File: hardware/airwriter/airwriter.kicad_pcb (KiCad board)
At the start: 2 copper layers, 62 x 104.3 mm, 130 parts, among them J1 USB-C 5V in, J2 Mini-DIN-8 to printer, J4 Mini-DIN-8 LocalTalk, SW1 EVQP44B3M side-press, SW3 TS-1002-BR16026, U1 ESP32-S3-WROOM-1-N8R2, U2 MAX3490ESA+, U3 MAX3232ESE+, U4 AP7361C-33E, U5 USBLC6-2SC6, U6 SP3485EN-L, U7 PIC12F1840-I/P, U8 SP3485EN-L, U9 74AHCT1G125SE-7

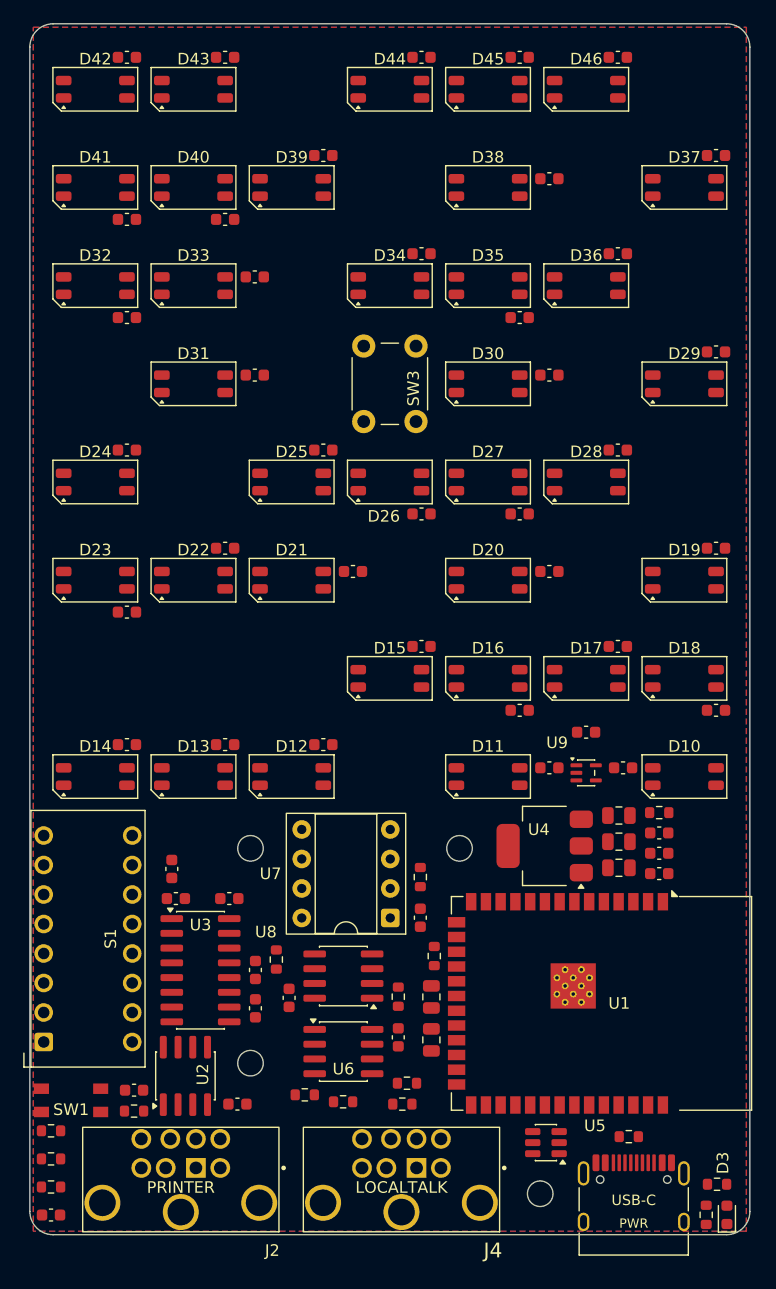
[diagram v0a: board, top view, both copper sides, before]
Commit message: Line the LED caps up for the light grille
All 37 bypass caps sit at one offset, 2.6mm north of their LED, inside
the grille cell and clear of the lattice walls; the LED designators
join the passives on F.Fab, which is what un-crowds the cells.

Refs: W-573
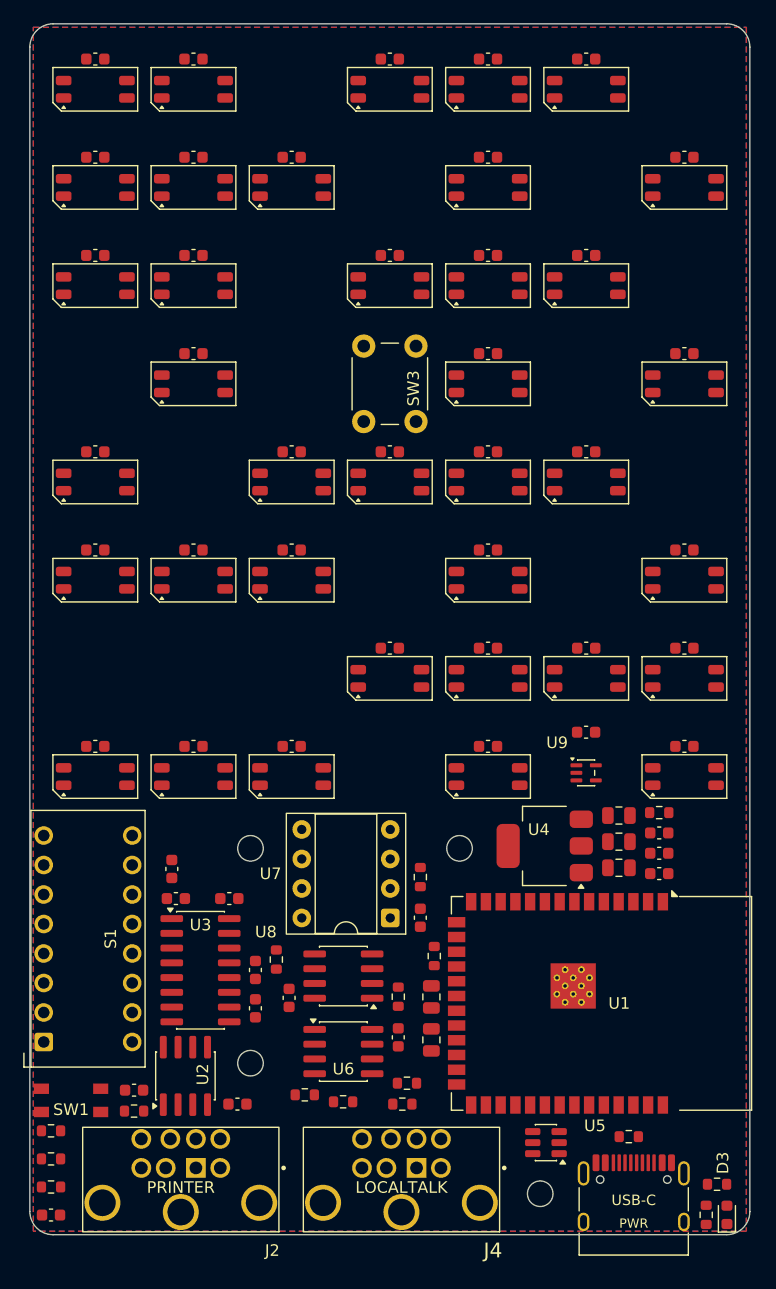
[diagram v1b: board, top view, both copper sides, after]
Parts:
- moved C38 6.00 mm to (156.4, 113.8)
- moved C55 6.00 mm to (139.5, 79.9)
- moved C60 6.00 mm to (114.1, 71.5)
- moved C36 6.00 mm to (139.5, 113.8)
- moved C46 6.00 mm to (131.0, 96.9)
- moved C47 6.00 mm to (139.5, 96.9)
- moved C52 6.00 mm to (105.6, 79.9)
- moved C61 6.00 mm to (105.6, 71.5)
- moved C43 6.00 mm to (105.6, 105.3)
- moved C30 5.59 mm to (156.4, 122.2)
- moved C31 5.59 mm to (139.5, 122.2)
- moved C53 5.59 mm to (114.1, 79.9)
- moved C58 5.59 mm to (139.5, 71.5)
- moved C40 5.59 mm to (139.5, 105.3)
- moved C41 5.59 mm to (122.5, 105.3)
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
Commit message: Route the dot-panel board
Full route at 60 passes, zero real breaks, 909 segments, 28 stitching
vias on the re-centred grid (stitch.py's lattice box now follows the
moved WROOM). Battery: 6 benign violations (5 silk-edge, U1's known
lib mismatch), drills at or above 0.30, /VBUS on the 0.5mm class.

Refs: W-573
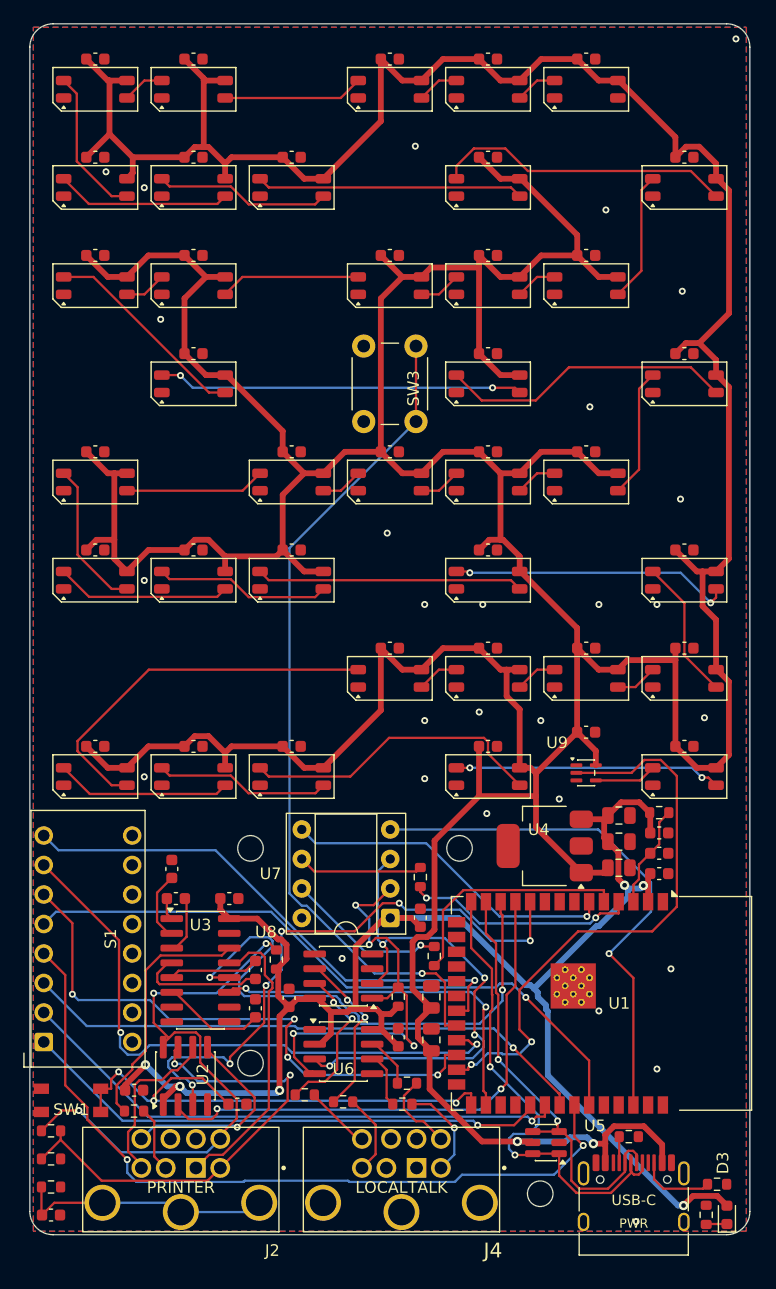
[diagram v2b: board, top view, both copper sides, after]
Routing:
- net /VBUS: track 0.00 -> 539.0 mm, vias 0 -> 2
- net /+3V3: track 0.00 -> 145.9 mm, vias 0 -> 6
- net /BTN_TEST: track 0.00 -> 72.9 mm, vias 0 -> 1
- net /DIP4: track 0.00 -> 66.6 mm, vias 0 -> 2
- net /DIP5: track 0.00 -> 56.8 mm, vias 0 -> 1
- net /DIP7: track 0.00 -> 52.3 mm, vias 0 -> 2
- net /UART_TX: track 0.00 -> 51.0 mm, vias 0 -> 6
- net /LED_DATA: track 0.00 -> 50.0 mm, vias 0 -> 2
- net /PR_TXD_P: track 0.00 -> 49.8 mm, vias 0 -> 3
- net /DIP6: track 0.00 -> 49.8 mm, vias 0 -> 4
- net /DIP3: track 0.00 -> 49.4 mm, vias 0 -> 1
- net /DIP2: track 0.00 -> 48.2 mm, vias 0 -> 1
- net /UART_CTS: track 0.00 -> 47.8 mm, vias 0 -> 2
- net /UART_RX: track 0.00 -> 46.6 mm, vias 0 -> 2
- net /DIP8: track 0.00 -> 46.1 mm, vias 0 -> 1
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
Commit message: Adjust silkscreen labels by hand
Wells repositioned silk labels in KiCad.

Refs: W-573
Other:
- board text added: "APPLETALK"
- board text added: "SERIAL"
- board text added: "TASHTALK"
- board text removed: "LOCALTALK"
- board text removed: "PRINTER"
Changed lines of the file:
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@@
 		(tags "SOIC SO 16-pin-NSOP R-16 R-16-S D0016A M2B SO16 SOT109-1 751B SOIC_N narrow")
 		(property "Reference" "U3"
-			(at 0 -3.9 0)
+			(at 0 0 0)
 			(layer "F.SilkS")
 			(effects
@@
 		(tags "SOIC SO")
 		(property "Reference" "U2"
-			(at 0.130733 1.494292 90)
+			(at 0 0 90)
 			(layer "F.SilkS")
 			(effects
@@
 		(tags "CMS SOT")
 		(property "Reference" "U4"
-			(at 0.51303 1.409538 180)
+			(at 3.135 2.695 180)
 			(layer "F.SilkS")
 			(effects
@@
 		(tags "SOIC SO")
 		(property "Reference" "U6"
-			(at 0 1.5 0)
+			(at 0 0 0)
 			(layer "F.SilkS")
 			(effects
@@
 		(tags "SOIC SO")
 		(property "Reference" "U8"
-			(at 6.678363 3.798133 180)
+			(at 0 0 180)
 			(layer "F.SilkS")
 			(effects
@@
 		(tags "SOT TO_SOT_SMD SC-88A SOT-353 SC-70-5")
 		(property "Reference" "U9"
-			(at -2.5 -2.598077 0)
+			(at -2.5 0 0)
 			(layer "F.SilkS")
 			(effects
@@
 		(tags "DIP switch SPST right angle piano DP-08RP 7.62mm 300mil")
 		(property "Reference" "S1"
-			(at 0 1.955 90)
+			(at 0 0 90)
 			(layer "F.SilkS")
 			(effects
@@
 		(tags "tactile switch side press edge mount EVQP4 C79164")
 		(property "Reference" "SW1"
-			(at 0 -0.8 180)
+			(at 0 0 180)
 			(layer "F.SilkS")
 			(effects
@@
 		(tags "THT DIP DIL PDIP 2.54mm 7.62mm 300mil Socket")
 		(property "Reference" "U7"
-			(at 10.31 3.81 180)
+			(at 3.81 3.81 180)
 			(layer "F.SilkS")
 			(effects
@@
 		(layer "Edge.Cuts")
 	)
-	(gr_text "PWR"
-		(at 152 163.3 0)
+	(gr_text "SERIAL"
+		(at 113 160.2 0)
 		(layer "F.SilkS")
 		(effects
 			(font
-				(size 0.8 0.8)
+				(size 1 1)
 				(thickness 0.15)
 			)
 		)
 	)
-	(gr_text "USB-C"
-		(at 152 161.3 0)
+	(gr_text "TASHTALK"
+		(at 127.2 127.4 0)
 		(layer "F.SilkS")
 		(effects
 			(font
-				(size 0.9 0.9)
+				(size 1 1)
 				(thickness 0.15)
 			)
 		)
 	)
-	(gr_text "PRINTER"
-		(at 113 160.2 0)
+	(gr_text "APPLETALK"
+		(at 132 160.2 0)
 		(layer "F.SilkS")
 		(effects
@@
 		)
 	)
-	(gr_text "LOCALTALK"
-		(at 132 160.2 0)
+	(gr_text "USB-C"
+		(at 152 160.4 0)
+		(layer "F.SilkS")
+		(effects
+			(font
+				(size 1 1)
+				(thickness 0.15)
+			)
+		)
+	)
+	(gr_text "PWR"
+		(at 152 162.12 0)
 		(layer "F.SilkS")
 		(effects

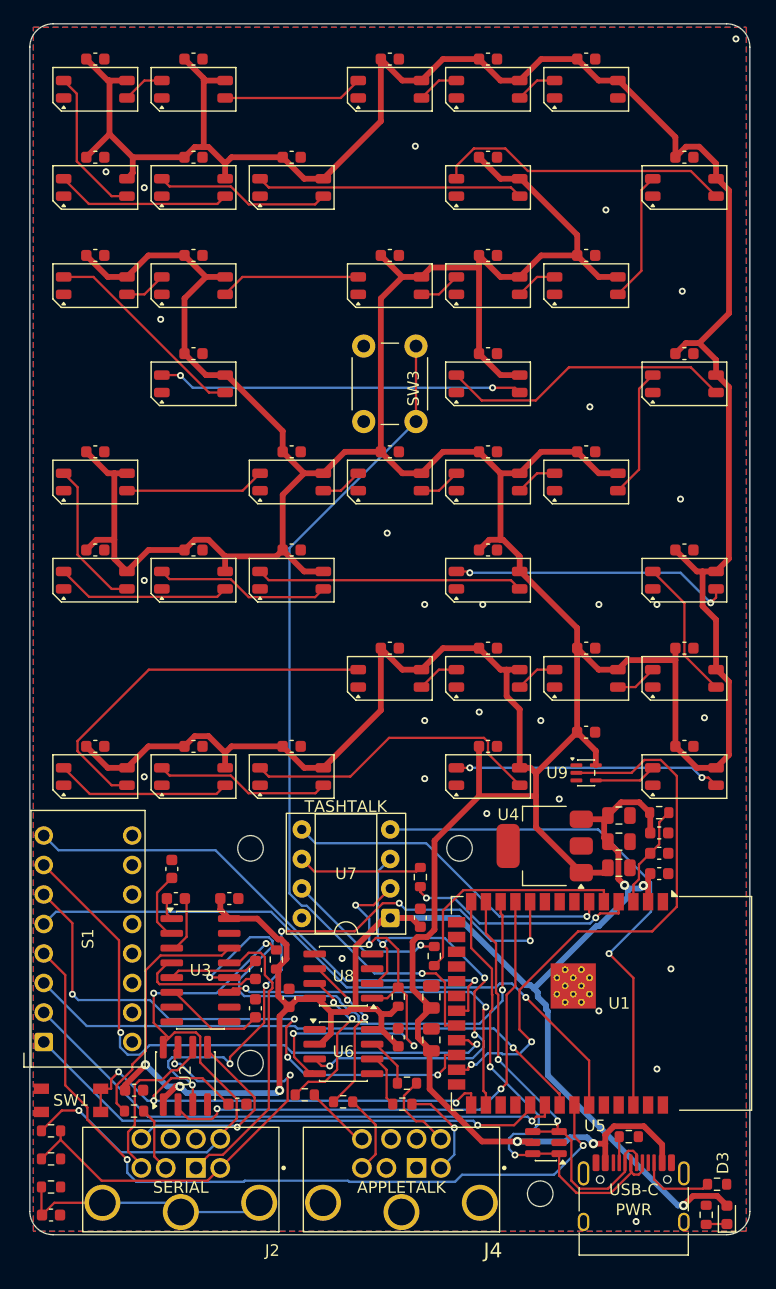
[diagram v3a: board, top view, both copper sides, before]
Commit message: Even the ports and fit the mounts for M2.5
Ports at 19.5mm centers (J4 to 132.5; J2's pocket had no slack so it
anchors). All four mounting holes drilled to 2.75mm for the M2.5
case-to-panel screw stack; H4 recentered between J4 and J1. Re-routed
clean: zero real breaks, 22 stitching vias. The five new
lib_footprint_mismatch entries are the enlarged holes, board-local by
design like U1's vias. The one silk overlap is Wells's own TASHTALK
label, left as placed.

Refs: W-573
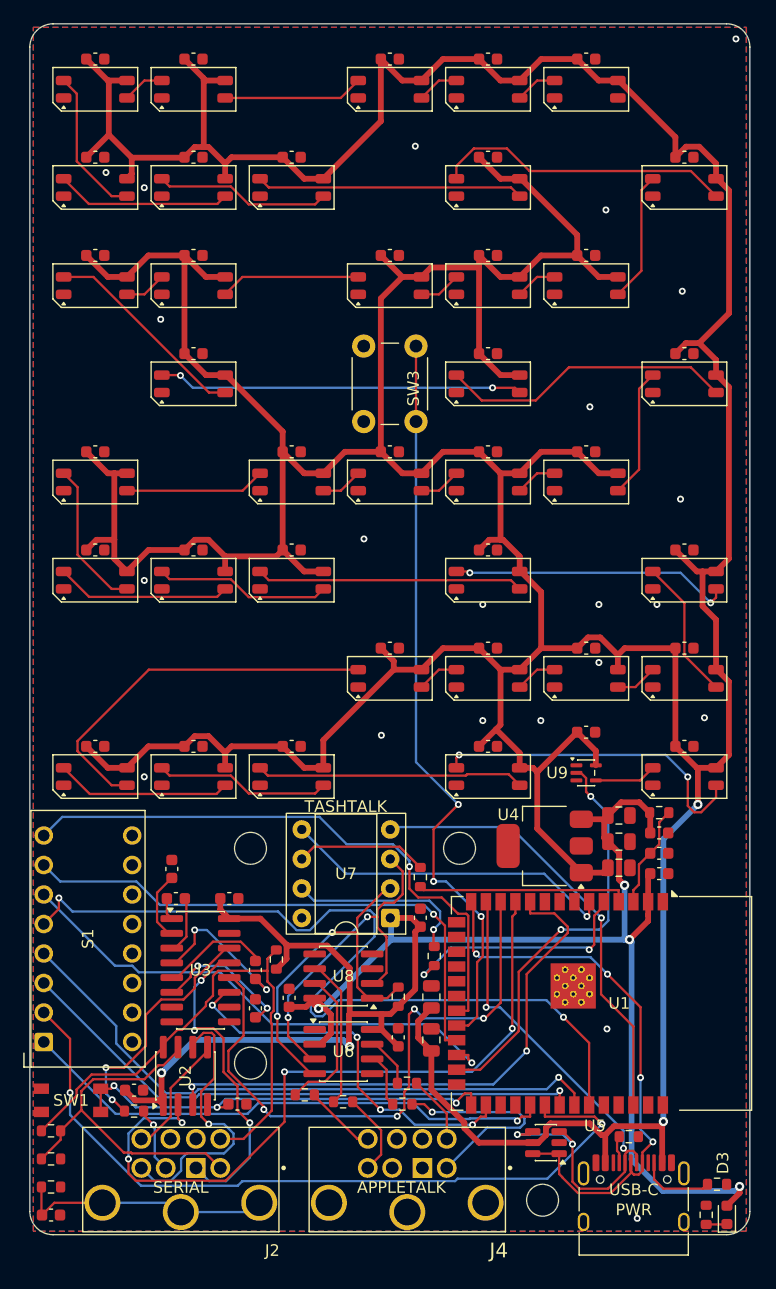
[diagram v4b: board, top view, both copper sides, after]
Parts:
- moved H4 0.59 mm to (144.2, 161.3)
- moved J4 0.50 mm to (132.5, 167.0)
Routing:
- net /+3V3: track 145.9 -> 164.8 mm
- net /DIP2: track 48.2 -> 66.5 mm, vias 1 -> 2
- net /DIP5: track 56.8 -> 74.2 mm, vias 1 -> 2
- net /UART_RX: track 46.6 -> 62.9 mm, vias 2 -> 4
- net /LED_DATA: track 50.0 -> 35.5 mm
- net /LT_DE: track 44.9 -> 30.7 mm, vias 4 -> 2
- net /DIP4: track 66.6 -> 53.7 mm, vias 2 -> 1
- net /LT_PORT_Y: track 8.42 -> 18.9 mm
- net /PR_TXD_N: track 41.6 -> 31.4 mm, vias 2 -> 0
- net /PR_RXD_N: track 14.6 -> 24.7 mm, vias 0 -> 1
- net /USB_DM: track 38.5 -> 47.7 mm, vias 2 -> 4
- net /BOOT_CFG: track 45.9 -> 37.7 mm
- net /BTN_TEST: track 72.9 -> 64.8 mm, vias 1 -> 3
- net /PR_RXD_P: track 18.0 -> 10.6 mm, vias 1 -> 0
- net /LT_RESET: track 45.9 -> 38.8 mm
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
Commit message: Spread the mounts to the corners
The LED field re-places onto Frame 9b's map -- 37 LEDs, serpentine
re-derived, worst error 0.0000mm, no schematic change -- and the four M2.5
holes leave the board's south half for its corners. Support hull 505mm2 ->
4069mm2, eight times the span.

  H1 (105.636,  65.636)  under panel dot (0,0), gold
  H2 (156.364,  65.636)  under panel dot (0,6), gold
  H3 (105.636, 151.930)  H1's column, as far south as J2 allows
  H4 (143.990, 160.830)  east, in the pocket between J4 and J1

THE LOWER PAIR CANNOT REACH THE LABEL RULE AT y=155, AND CANNOT SHARE A y.
Both are arithmetic and r7_anchors.py prints them on every run. West: J2's
courtyard starts at y=154.675 and spans x 104.205..121.795, so a 4.882mm
courtyard clearing it caps H3 at y <= 152.034 -- 2.97mm short, against
1.5mm of freedom. East: U1's courtyard ends at y=153.845 so the hole needs
y >= 156.486, and J1's starts at y=156.855 so it needs y <= 154.214. The
band is empty at every point on that column.

Nudging east does not rescue it, and the authorisation for it rests on a
fact that changed. J1 reaches x=157.315, so any hole overlapping it in x is
still capped at y <= 154.214, and the WROOM's antenna occupies x
156.0..162.0, y 135.35..153.35 -- a 2.75mm drill at that y reaches 152.84,
0.51mm UNDER the radiating element. Clearing J1 in x instead needs a centre
at x >= 159.96, whose courtyard runs off the board. There is no antenna
overhang any more; Wells ruled the module flush in round 6 and it sits over
solid board. Metal under the radiator is a different question from metal
under an overhang, so H4 stays in the J4/J1 pocket and the call goes back.

The west edge is one stack now, pinned at J2 and packed upward at 0.3mm:
S1 to y=134.32, SW1 to y=147.50, then H3. Only y moved -- the DIP's body
face is still 0.20mm off x=100 with its keys outboard, and the reset
actuator is still flush at x=100.000. S1 reaches 4.465mm into the grid
zone, which is what Frame 9b's gold (7,0) bought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
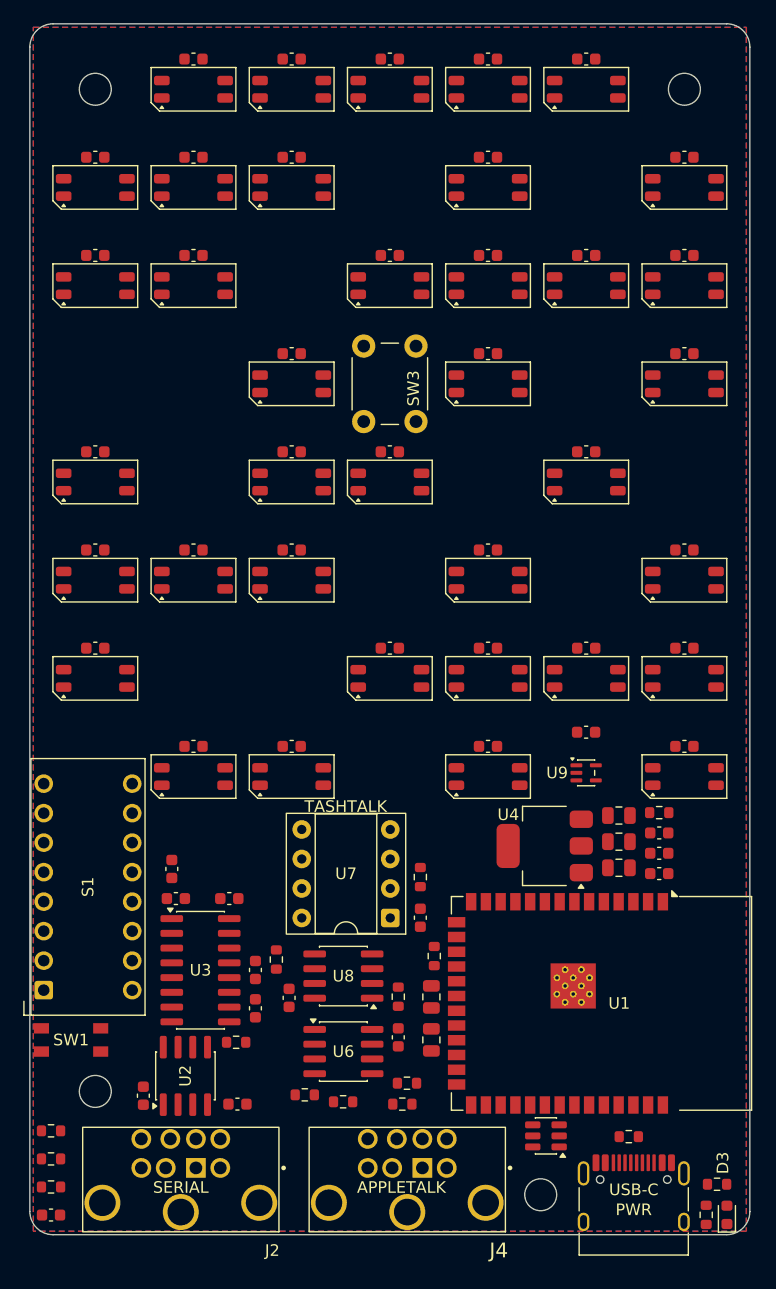
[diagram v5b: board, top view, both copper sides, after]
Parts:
- moved H2 68.2 mm to (156.4, 65.6)
- moved H1 66.7 mm to (105.6, 65.6)
- moved C49 16.9 mm to (139.5, 88.4)
- moved D29 16.9 mm to (139.5, 91.0)
- moved C53 16.9 mm to (131.0, 79.9)
- moved D33 16.9 mm to (131.0, 82.5)
- moved C50 16.9 mm to (122.5, 88.4)
- moved D30 16.9 mm to (122.5, 91.0)
- moved H3 13.6 mm to (105.6, 151.9)
- moved C48 12.0 mm to (156.4, 88.4)
- moved D28 12.0 mm to (156.4, 91.0)
- moved C51 12.0 mm to (105.6, 79.9)
- moved D31 12.0 mm to (105.6, 82.5)
- moved R9 10.6 mm to (117.8, 147.7)
- moved C56 8.46 mm to (156.4, 79.9)
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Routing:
- net /VBUS: track 542.9 -> 0.00 mm, vias 2 -> 0
- net /+3V3: track 164.8 -> 0.00 mm, vias 6 -> 0
- net /DIP5: track 74.2 -> 0.00 mm, vias 2 -> 0
- net /DIP2: track 66.5 -> 0.00 mm, vias 2 -> 0
- net /BTN_TEST: track 64.8 -> 0.00 mm, vias 3 -> 0
- net /UART_RX: track 62.9 -> 0.00 mm, vias 4 -> 0
- net /DIP4: track 53.7 -> 0.00 mm, vias 1 -> 0
- net /UART_CTS: track 52.4 -> 0.00 mm, vias 4 -> 0
- net /DIP8: track 51.3 -> 0.00 mm, vias 1 -> 0
- net /DIP3: track 50.0 -> 0.00 mm, vias 1 -> 0
- net /USB_DP: track 49.3 -> 0.00 mm, vias 4 -> 0
- net /UART_TX: track 48.6 -> 0.00 mm, vias 2 -> 0
- net /USB_DM: track 47.7 -> 0.00 mm, vias 4 -> 0
- net /DIP7: track 47.6 -> 0.00 mm, vias 1 -> 0
- net /PR_TXD_P: track 46.7 -> 0.00 mm
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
